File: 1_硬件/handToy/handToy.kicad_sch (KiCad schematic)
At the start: 35 parts

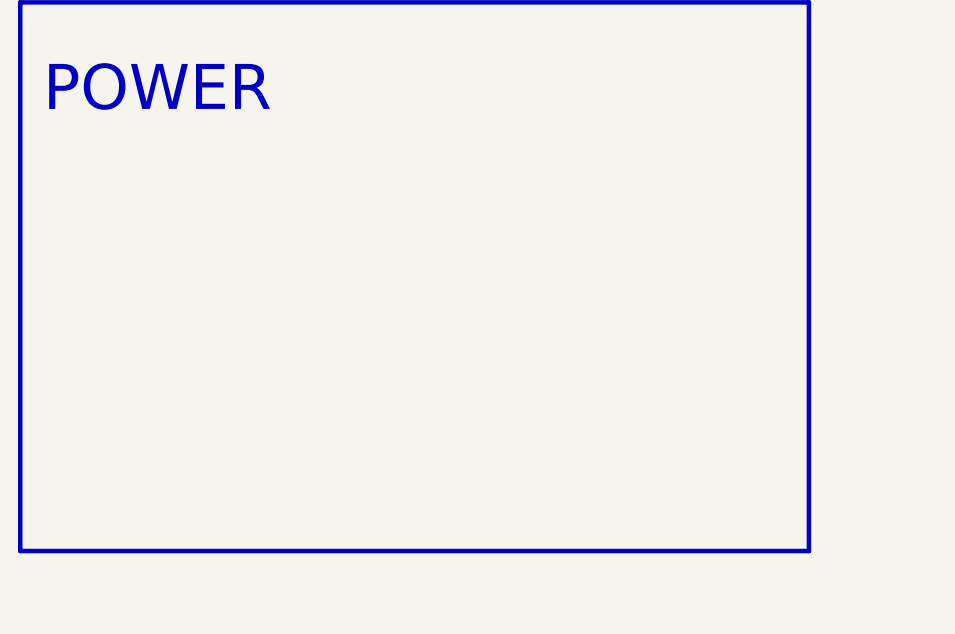
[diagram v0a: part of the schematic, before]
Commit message: 硬件：增加电池管理电路
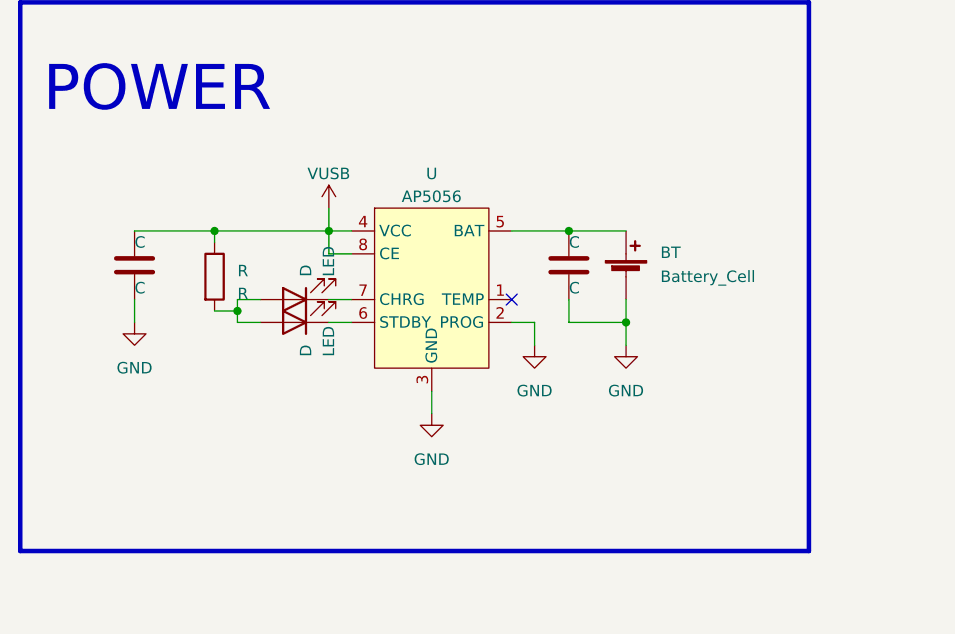
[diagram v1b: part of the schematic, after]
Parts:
- added BT: Battery_Cell, symbol Device:Battery_Cell
- added C (x2): C, symbol Device:C
- added D (x2): LED, symbol Device:LED
- added R: R, symbol Device:R
- added U: AP5056, symbol Power-one2inf:AP5056
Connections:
- net GND: now also BT.2 (-), C.2, C.2, U.2 (PROG), U.3 (GND)
- net VUSB: now also C.1, R.1, U.4 (VCC), U.8 (CE)
- new net: BT.1 (+), C.1, U.5 (BAT)
- new net: D.2 (A), D.2 (A), R.2
- new net: D.1 (K), U.6 (STDBY)
- new net: D.1 (K), U.7 (CHRG)
- no-connect marks 28 -> 29
